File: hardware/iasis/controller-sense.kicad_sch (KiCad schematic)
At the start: 28 parts, among them U1141 TMUX1511PWR, U1142 TMUX1511PWR

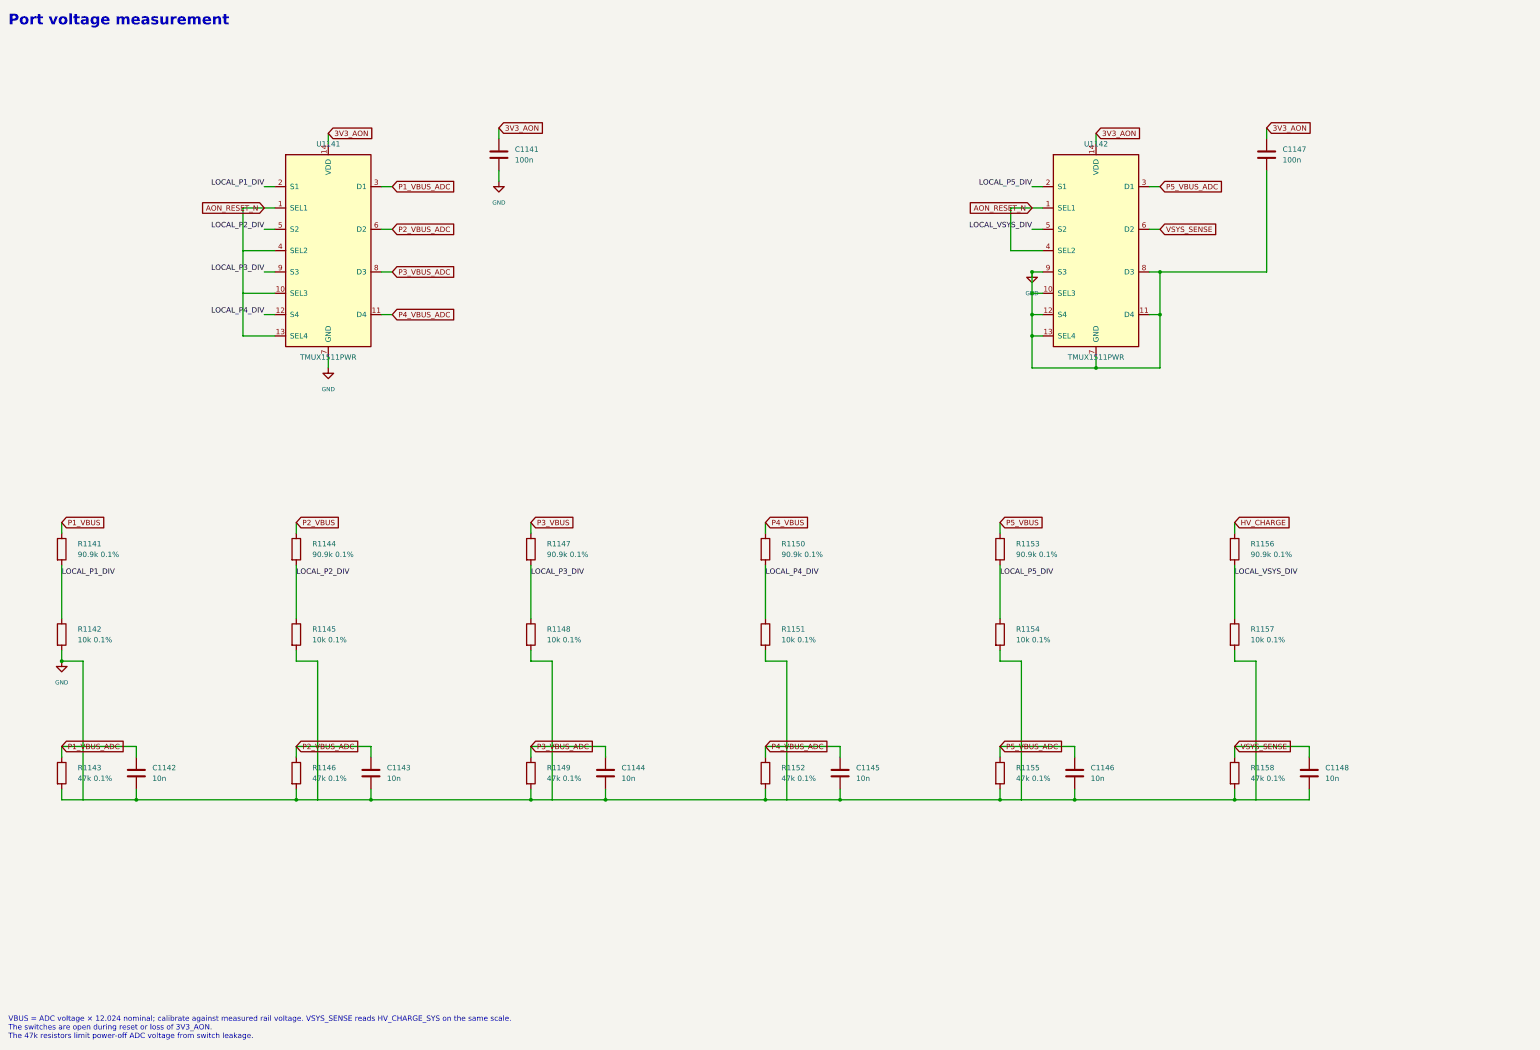
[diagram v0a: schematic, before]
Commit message: Wire the schematic islands and side-match the RP2354 GPIOs
Each sheet now draws its circuits with wires. Labels remain at block edges
and on single-part islands: buttons, test points, decoupling and pull
resistors. The target-port page wires its hierarchical labels straight to
the child sheet pins, the ports page points its labels away from each
block, and the root sheet keeps every block clear of the title block.

The RP2354B GPIOs are reassigned so each signal leaves the package on the
side facing its destination. Update PCB from Schematic applied the 43
U1101 pad-net changes with no geometry change. Otherwise the netlist
matches the previous design, ERC keeps its 14 existing warnings and DRC
reports no parity issues.
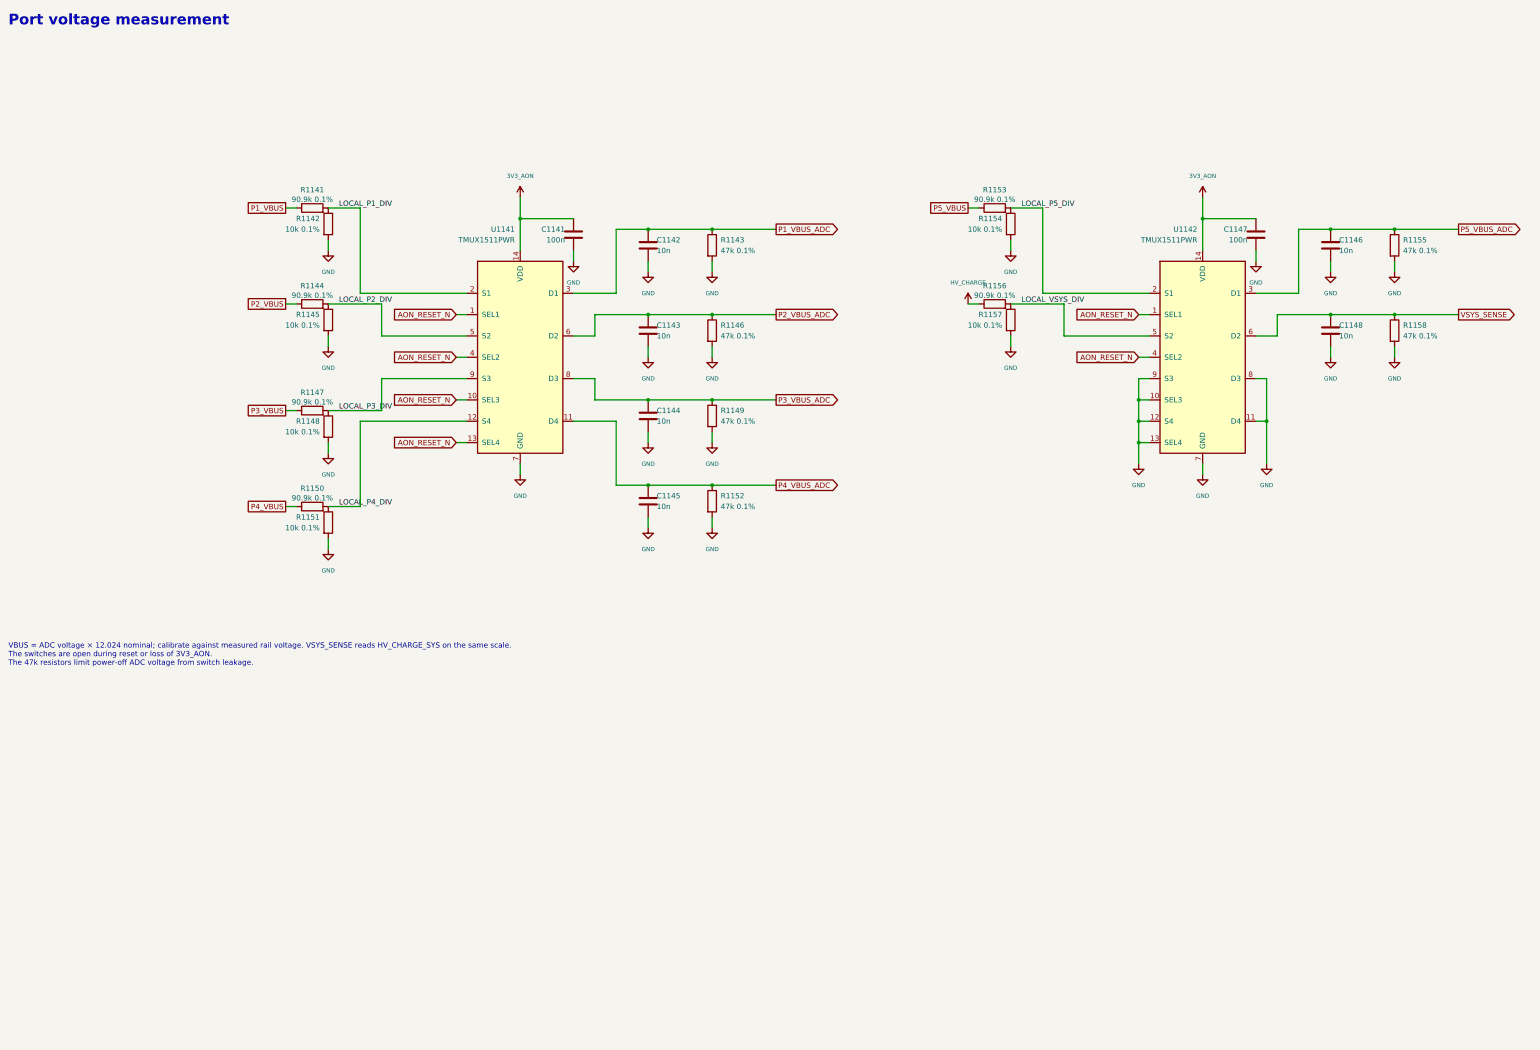
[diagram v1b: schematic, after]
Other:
- moved on the sheet: C1141, C1142, C1143, C1144, C1145, C1146, C1147, C1148, R1141, R1142, R1143, R1144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

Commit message: Redraw the controller support sheets
The management bus, indicator, power-control, voltage-measurement and
temperature sheets read left to right, with supplies up, ground down
and decoupling beside each IC. Pull resistors, test points and buttons
are labelled islands; everything else is wired. Supply rails use power
symbols with their existing net names, fields sit clear of bodies,
wires and text, and each sheet carries a title, date and revision. The
netlist is unchanged.
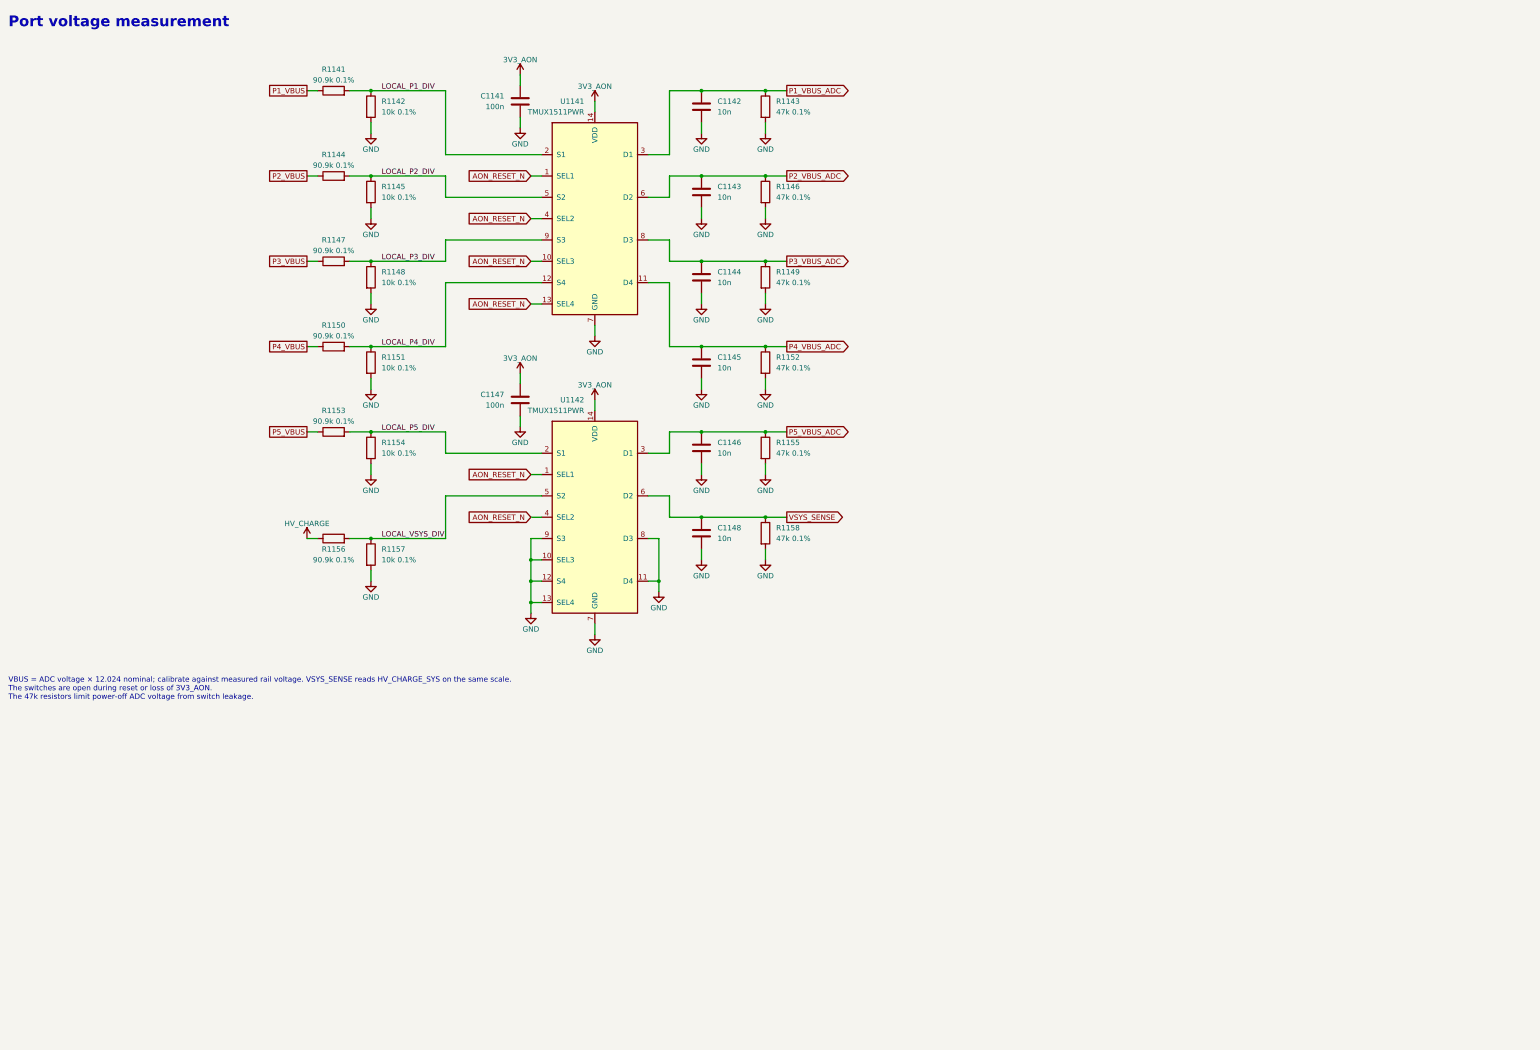
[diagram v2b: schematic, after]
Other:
- title: (none) -> Port voltage measurement
- moved on the sheet: C1141, C1142, C1143, C1144, C1145, C1146, C1147, C1148, R1141, R1142, R1143, R1144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
